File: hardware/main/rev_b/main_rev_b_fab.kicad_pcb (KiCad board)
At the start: 4 copper layers, 140 x 100 mm, 165 parts, among them J1 USB-C USB2, J10 SWD, J2 ESC_CAN_POWER, J30 GNSS_UFL, J40 915MHz_ANT, Q30 2N7002, U1 USBLC6-2SC6, U10 RP2354B, U2 TLV62569DBVR, U20 ICM-42688-P, U21 LSM6DSO32TR, U22 LPS22DFTR, U3 TLV75528PDBVR, U30 LG77LICMD, U4 TLV75533PDBVR, U40 CC1121RHBR, U41 CC1190RGVR, U50 TCAN3413DR, U51 MCP2518FD-H/QBB, Y1 12MHz ABM8-272-T3, Y40 32MHz NT2016SA-32M-TEE3017A, Y50 40MHz ABM8G

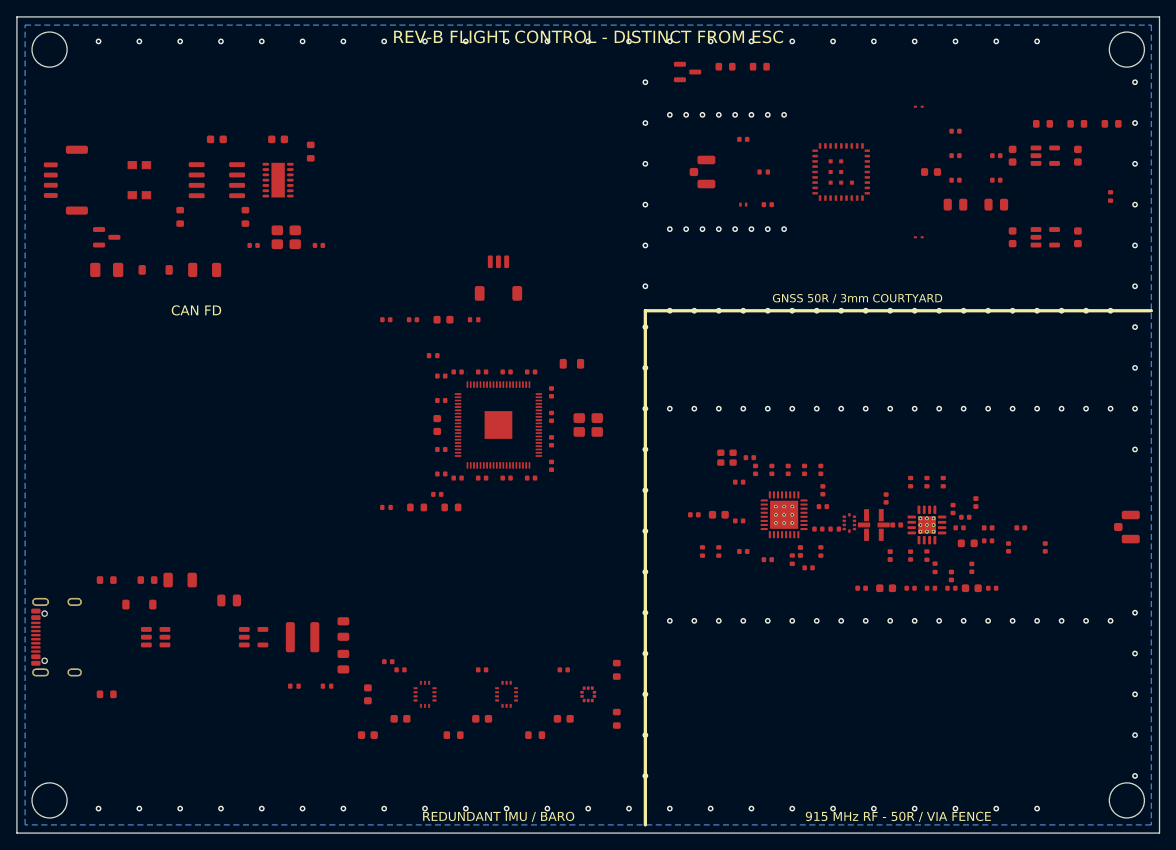
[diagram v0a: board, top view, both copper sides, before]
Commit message: build: route and validate rev-b boards
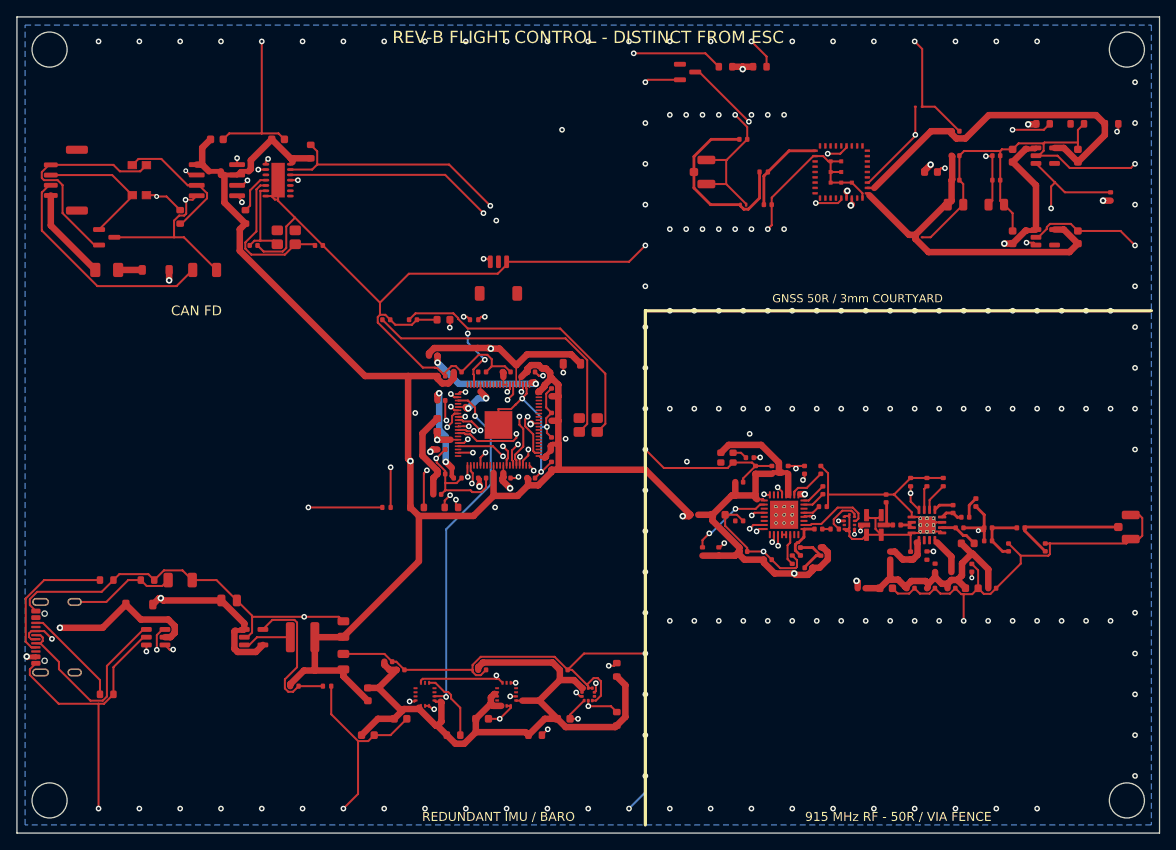
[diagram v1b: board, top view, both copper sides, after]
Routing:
- net /GND: track 0.00 -> 1404.1 mm, vias 154 -> 170
- net /3V3: track 0.00 -> 312.4 mm, vias 0 -> 8
- net /SYS_5V: track 0.00 -> 184.8 mm, vias 0 -> 3
- net /GNSS_RX: track 0.00 -> 104.0 mm, vias 0 -> 3
- net /GNSS_PWR_EN: track 0.00 -> 96.2 mm, vias 0 -> 3
- net /Redundant sensors/3V3_SENS: track 0.00 -> 92.1 mm
- net /GNSS_PPS: track 0.00 -> 77.9 mm, vias 0 -> 3
- net /1V1: track 0.00 -> 74.0 mm, vias 0 -> 6
- net /GNSS/GNSS_RESET_OD: track 0.00 -> 72.9 mm, vias 0 -> 3
- net /915 MHz RF/VDD_CC112: track 0.00 -> 68.0 mm, vias 0 -> 2
- net /GNSS_TX: track 0.00 -> 66.7 mm, vias 0 -> 2
- net /CAN_nCS: track 0.00 -> 65.0 mm, vias 0 -> 2
- net /SENS_MOSI: track 0.00 -> 63.3 mm, vias 0 -> 3
- net /CAN_MISO: track 0.00 -> 60.9 mm, vias 0 -> 2
- net /PA_EN: track 0.00 -> 59.6 mm, vias 0 -> 2
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
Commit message: build: route and validate rev-b boards
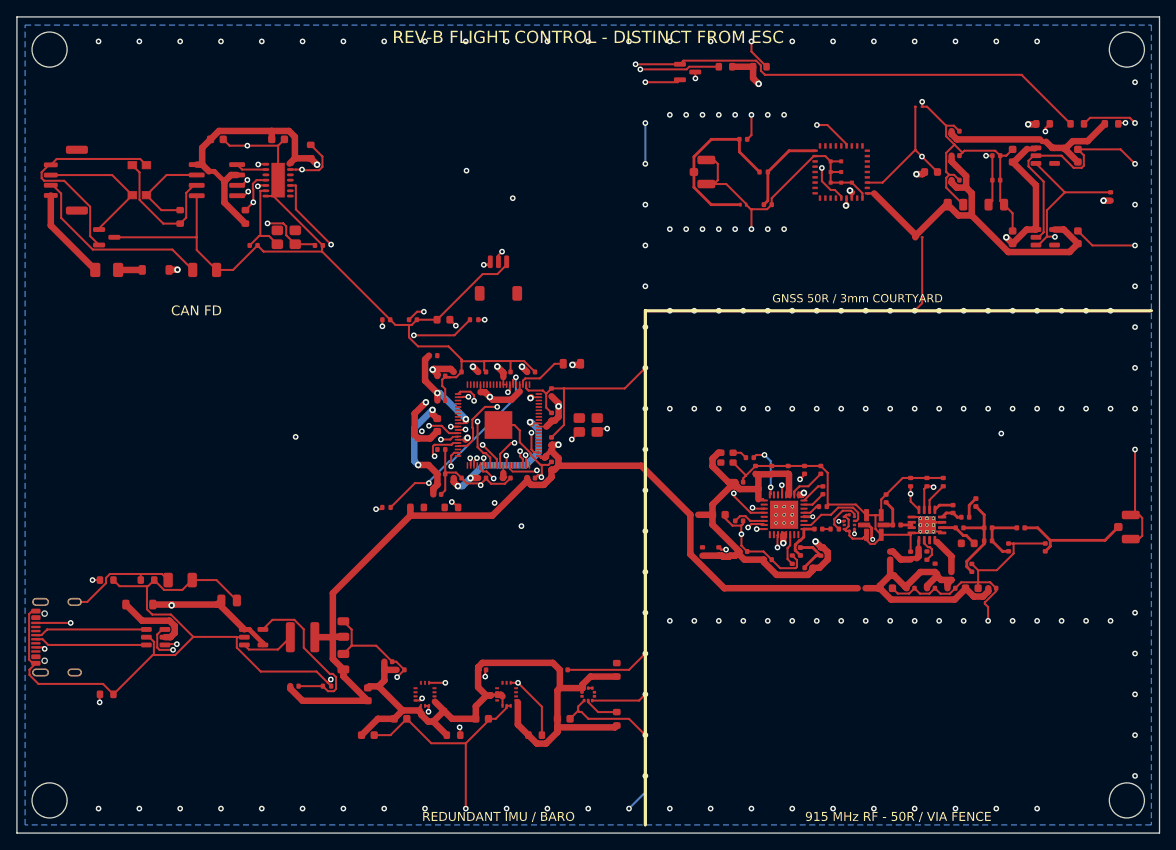
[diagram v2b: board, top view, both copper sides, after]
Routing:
- net /GNSS_RESET_N: track 0.00 -> 115.5 mm, vias 0 -> 2
- net /GND: track 1404.1 -> 1325.5 mm, vias 170 -> 164
- net /SENS_MOSI: track 63.3 -> 0.00 mm, vias 3 -> 0
- net /CAN_INT: track 5.11 -> 67.5 mm, vias 0 -> 3
- net /CAN_MISO: track 60.9 -> 0.00 mm, vias 2 -> 0
- net /CAN_MOSI: track 59.1 -> 0.00 mm, vias 3 -> 0
- net /LNA_EN: track 3.01 -> 61.5 mm, vias 0 -> 2
- net /LSM_INT2: track 55.7 -> 0.00 mm, vias 2 -> 0
- net /BARO_SCL: track 55.6 -> 0.00 mm, vias 4 -> 0
- net /CAN_SCK: track 0.00 -> 48.3 mm, vias 0 -> 2
- net /RF_GPIO0: track 44.0 -> 0.00 mm, vias 2 -> 0
- net /RF_GPIO3: track 0.00 -> 44.0 mm, vias 0 -> 3
- net /BARO_SDA: track 47.4 -> 4.20 mm, vias 2 -> 0
- net /ICM_INT2: track 42.4 -> 0.00 mm, vias 2 -> 0
- net /BARO_DRDY: track 41.3 -> 0.00 mm, vias 2 -> 0
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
